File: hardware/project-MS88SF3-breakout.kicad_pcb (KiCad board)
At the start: 2 copper layers, 25.4 x 30.5 mm, 27 parts, among them J1 Conn_02x05_Odd_Even, J2 SM04B-SRSS-TB(LF)(SN), J3 USB4105-GF-A, J4 Conn_01x06_Male, J5 Conn_01x08_Male, SW1 SW_SPST, U1 MS88SF3

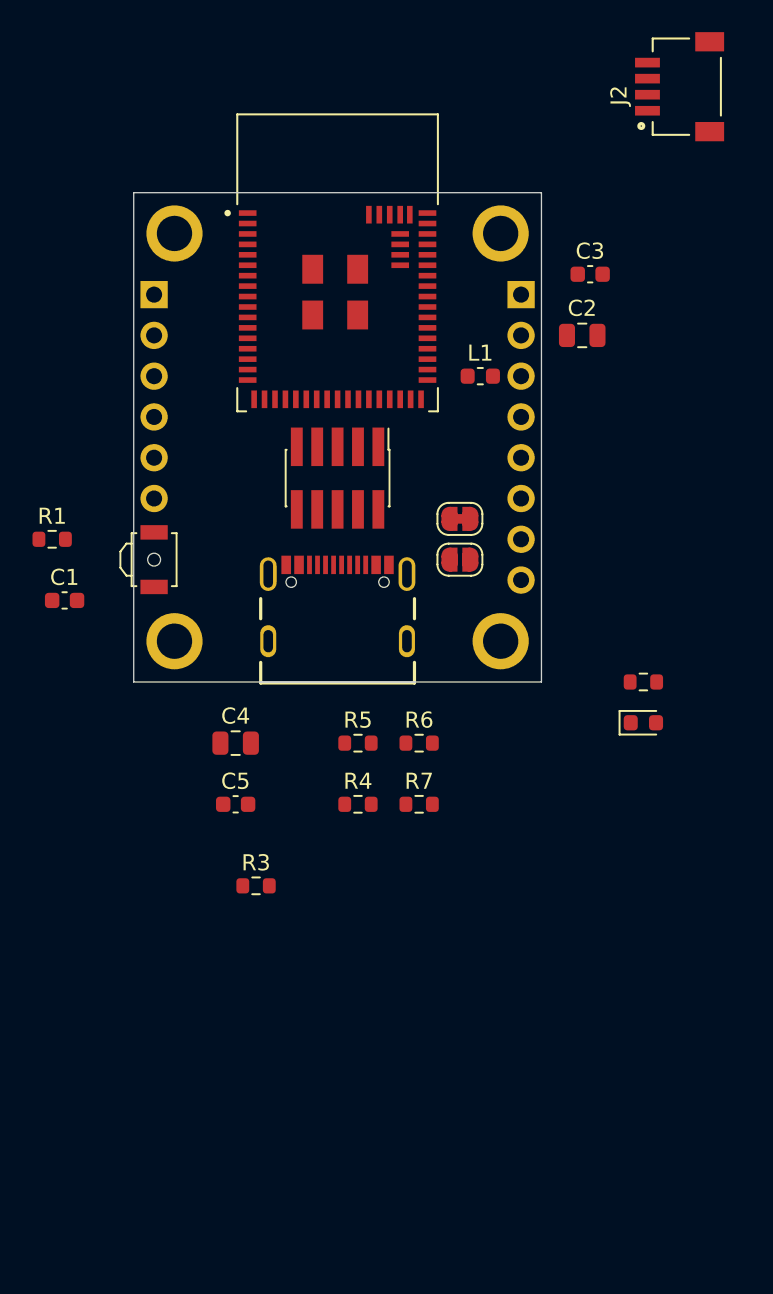
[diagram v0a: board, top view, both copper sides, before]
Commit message: Make it a feather shape
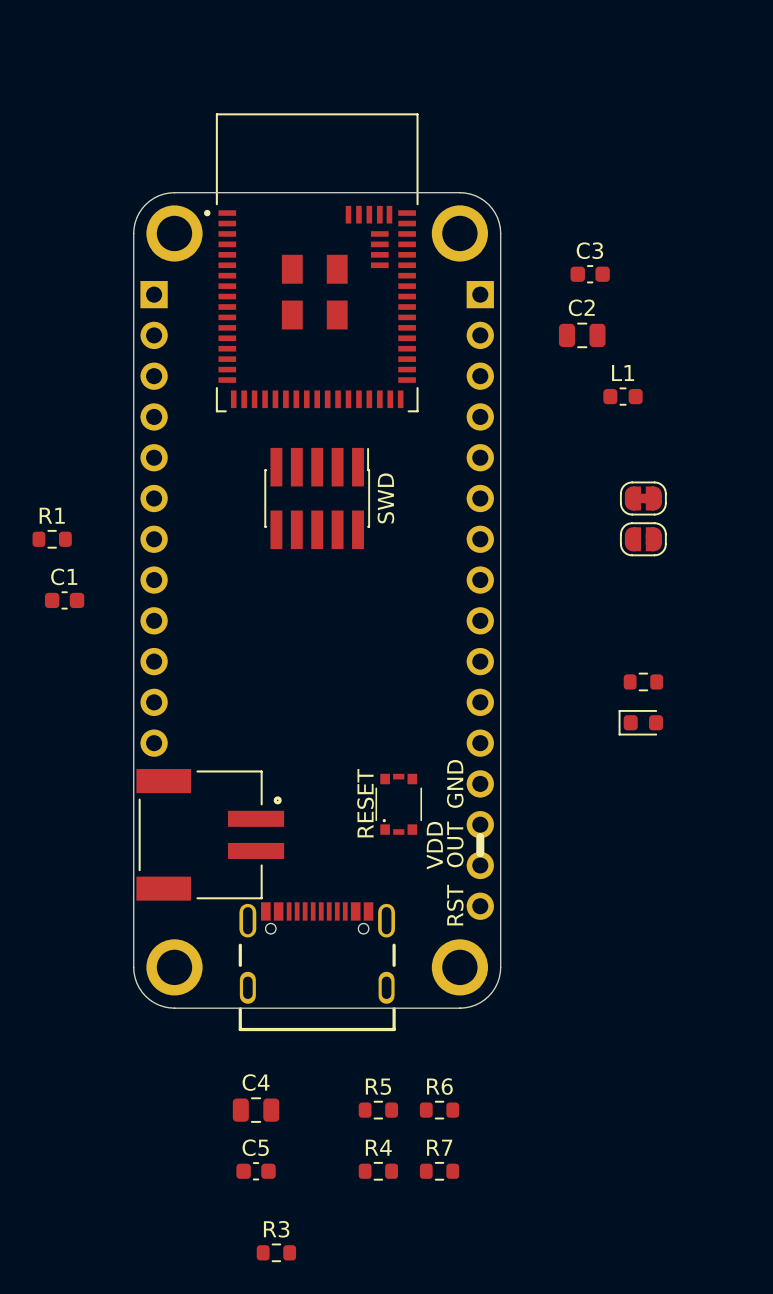
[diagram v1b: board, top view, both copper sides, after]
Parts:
- removed SW1: SW_SPST, Button_Switch_SMD:SW_SPST_B3U-3000P-B
- added S1: 435151014824, 435151014824:435151014824, F.Cu at (52.6, 118.9)
- J2: value SM04B-SRSS-TB(LF)(SN) -> S2B-PH-SM4-TB(LF)(SN); footprint SM04B-SRSS-TB(LF)(SN):JST_SM04B-SRSS-TB(LF)(SN) -> S2B-PH-SM4-TB(LF)(SN):JST_S2B-PH-SM4-TB(LF)(SN)
- J4: value Conn_01x06_Male -> Conn_01x12_Male; footprint Connector_PinHeader_2.54mm:PinHeader_1x06_P2.54mm_Vertical -> Connector_PinHeader_2.54mm:PinHeader_1x12_P2.54mm_Vertical; moved to B.Cu
- J5: value Conn_01x08_Male -> Conn_01x16_Male; footprint Connector_PinHeader_2.54mm:PinHeader_1x08_P2.54mm_Vertical -> Connector_PinHeader_2.54mm:PinHeader_1x16_P2.54mm_Vertical; moved to B.Cu
- moved J2 52.6 mm to (43.7, 120.8), turned to 270 degrees
- moved R3 22.9 mm to (45.0, 146.8)
- moved C4 22.9 mm to (43.7, 137.9)
- moved C5 22.9 mm to (43.7, 141.7)
- moved R4 22.9 mm to (51.3, 141.7)
- moved R5 22.9 mm to (51.3, 137.9)
- moved R6 22.9 mm to (55.1, 137.9)
- moved R7 22.9 mm to (55.1, 141.7)
- moved J3 21.6 mm to (47.5, 130.3)
- moved H4 20.5 mm to (56.4, 129.0)
- moved H3 20.3 mm to (38.6, 129.0)
- moved JP2 11.5 mm to (67.8, 102.4)
- moved JP1 11.5 mm to (67.8, 99.8)
- moved L1 8.98 mm to (66.5, 93.5)
- moved H2 2.54 mm to (56.4, 83.3)
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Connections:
- net Net-(JP1-Pad2) renamed /VDDH
- net Net-(U1-Pad49) renamed /SWDIO
- net Net-(U1-Pad50) renamed /SWCLK
- C1 pad 1: Net-(C1-Pad1) -> /RESET
- C1 pad 2: Net-(C1-Pad2) -> GND
- C2 pad 1: Net-(C2-Pad1) -> /VDD_nRF
- C2 pad 2: Net-(C2-Pad2) -> GND
- C3 pad 1: Net-(C3-Pad1) -> /VDD_nRF
- C3 pad 2: Net-(C3-Pad2) -> GND
- C4 pad 1: Net-(C4-Pad1) -> /VBUS
- C4 pad 2: Net-(C4-Pad2) -> GND
- C5 pad 1: Net-(C5-Pad1) -> /VBUS
- C5 pad 2: Net-(C5-Pad2) -> GND
- D1 pad 1: Net-(D1-Pad1) -> GND
- H1 pad 1: Net-(H1-Pad1) -> GND
- H2 pad 1: Net-(H2-Pad1) -> GND
- H3 pad 1: Net-(H3-Pad1) -> GND
- H4 pad 1: Net-(H4-Pad1) -> GND
- J1 pad 1: Net-(J1-Pad1) -> /VDD_nRF
- J1 pad 10: Net-(J1-Pad10) -> /RESET
- J1 pad 9: Net-(J1-Pad9) -> GND
- J3 pad A1_B12: Net-(J3-PadA1_B12) -> GND
- J3 pad A4_B9: Net-(J3-PadA4_B9) -> /VBUS
- J3 pad A5: Net-(J3-PadA5) -> /CC1
- J3 pad A6: Net-(J3-PadA6) -> /D+
- J3 pad A7: Net-(J3-PadA7) -> /D-
- J3 pad B1_A12: Net-(J3-PadA1_B12) -> GND
- J3 pad B4_A9: Net-(J3-PadA4_B9) -> /VBUS
- J3 pad B5: Net-(J3-PadB5) -> /CC2
- J3 pad B6: Net-(J3-PadB6) -> /D+
- J3 pad B7: Net-(J3-PadB7) -> /D-
- J3 pad S1: Net-(J3-PadS1) -> GND
- J3 pad S2: Net-(J3-PadS1) -> GND
- J3 pad S3: Net-(J3-PadS1) -> GND
- J3 pad S4: Net-(J3-PadS1) -> GND
- JP2 pad 1: /VDD_OUT -> /VDD_nRF
- L1 pad 2: /VDD_OUT -> /VDD_nRF
- R1 pad 1: Net-(R1-Pad1) -> /VDD_nRF
- R1 pad 2: Net-(R1-Pad2) -> /RESET
- R2 pad 1: Net-(R2-Pad1) -> Net-(D1-Pad2)
- R2 pad 2: Net-(R2-Pad2) -> /VBUS
- R3 pad 1: /VBUS_nRF -> /VBUS
- R3 pad 2: /VBUS_CONN -> /VBUS_nRF
- R4 pad 1: Net-(R4-Pad1) -> /CC1
- R4 pad 2: Net-(R4-Pad2) -> GND
- R5 pad 1: Net-(R5-Pad1) -> /CC2
- R5 pad 2: Net-(R5-Pad2) -> GND
- R6 pad 1: Net-(R6-Pad1) -> /D_P
- R6 pad 2: Net-(R6-Pad2) -> /D+
- R7 pad 1: Net-(R7-Pad1) -> /D_N
- R7 pad 2: Net-(R7-Pad2) -> /D-
- U1 pad 31: /VDD_OUT -> /VDD_nRF
- U1 pad 36: Net-(U1-Pad36) -> /D_N
- U1 pad 37: Net-(U1-Pad37) -> /D_P
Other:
- board size 25.4 x 30.5 mm -> 22.9 x 50.8 mm
- board text added: "GND"
- board text added: "OUT"
- board text added: "RESET"
- board text added: "RST"
- board text added: "SWD"
- board text added: "VDD"

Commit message: Change the MS88SF3 module to the nRF52840
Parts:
- U1: value MS88SF3 -> MS88SF3_NRF52840; footprint MS88SF3:MODULE_MS88SF3 -> MS88SF3_NRF52840:MODULE_MS88SF3_NRF52840
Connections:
- U1 pad 33: Net-(U1-Pad2) -> /DCCH
- U1 pad 38: Net-(U1-Pad2) -> Net-(U1-Pad38)
- U1 pad 43: Net-(U1-Pad2) -> Net-(U1-Pad43)
- U1 pad 48: Net-(U1-Pad2) -> Net-(U1-Pad48)
- U1 pad 58: Net-(U1-Pad2) -> Net-(U1-Pad58)
- U1 pad 60: Net-(U1-Pad2) -> Net-(U1-Pad60)

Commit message: Everything connected
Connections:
- net Net-(J4-Pad3) renamed /AIN1
- net Net-(U1-Pad2) renamed /P1.11
- net Net-(U1-Pad3) renamed /P1.12
- J1 pad 2: Net-(J1-Pad2) -> /SWDIO
- J1 pad 3: Net-(J1-Pad3) -> GND
- J1 pad 4: Net-(J1-Pad4) -> /SWCLK
- J1 pad 5: Net-(J1-Pad5) -> GND
- J1 pad 6: Net-(J1-Pad6) -> /TX
- J1 pad 8: Net-(J1-Pad8) -> /RX
- J2 pad 1: Net-(J2-Pad1) -> /VDD_nRF
- J2 pad 2: Net-(J2-Pad2) -> GND
- J2 pad S1: Net-(J2-PadS1) -> GND
- J2 pad S2: Net-(J2-PadS1) -> GND
- J4 pad 1: Net-(J4-Pad1) -> /P1.10
- J4 pad 10: Net-(J4-Pad10) -> /VBUS
- J4 pad 12: Net-(J4-Pad12) -> /VDD_nRF
- J4 pad 2: Net-(J4-Pad2) -> /P1.14
- J4 pad 4: Net-(J4-Pad4) -> /P1.13
- J4 pad 5: Net-(J4-Pad5) -> /P1.15
- J4 pad 6: Net-(J4-Pad6) -> /AIN0
- J4 pad 7: Net-(J4-Pad7) -> /AIN5
- J4 pad 8: Net-(J4-Pad8) -> /AIN3
- J4 pad 9: Net-(J4-Pad9) -> /AIN2
- J5 pad 1: Net-(J5-Pad1) -> /NFC1
- J5 pad 10: Net-(J5-Pad10) -> /P0.15
- J5 pad 11: Net-(J5-Pad11) -> /P0.13
- J5 pad 12: Net-(J5-Pad12) -> /P0.19
- J5 pad 13: Net-(J5-Pad13) -> GND
- J5 pad 14: Net-(J5-Pad14) -> /VDD_nRF
- J5 pad 15: Net-(J5-Pad15) -> /VDD_nRF
- J5 pad 16: Net-(J5-Pad16) -> /RESET
- J5 pad 2: Net-(J5-Pad2) -> /NFC2
- J5 pad 3: Net-(J5-Pad3) -> /TX
- J5 pad 4: Net-(J5-Pad4) -> /RX
- J5 pad 5: Net-(J5-Pad5) -> /P0.25
- J5 pad 6: Net-(J5-Pad6) -> /P0.22
- J5 pad 7: Net-(J5-Pad7) -> /P0.23
- J5 pad 8: Net-(J5-Pad8) -> /P0.21
- J5 pad 9: Net-(J5-Pad9) -> /P0.17
- L1 pad 1: /DCCH -> /VDD_nRF
- L1 pad 2: /VDD_nRF -> /DCCH
- U1 pad 10: Net-(U1-Pad10) -> /AIN5
- U1 pad 15: Net-(U1-Pad15) -> /AIN3
- U1 pad 16: Net-(U1-Pad16) -> /AIN2
- U1 pad 38: Net-(U1-Pad38) -> /P0.19
- U1 pad 39: Net-(U1-Pad39) -> /P0.13
- U1 pad 4: Net-(U1-Pad4) -> /P1.10
- U1 pad 40: Net-(U1-Pad40) -> /P0.15
- U1 pad 41: Net-(U1-Pad41) -> /P0.17
- U1 pad 42: Net-(U1-Pad42) -> /P0.21
- U1 pad 43: Net-(U1-Pad43) -> /P0.23
- U1 pad 45: Net-(U1-Pad45) -> /P0.22
- U1 pad 48: Net-(U1-Pad48) -> /P0.25
- U1 pad 5: Net-(U1-Pad5) -> /P1.14
- U1 pad 55: Net-(U1-Pad55) -> /NFC1
- U1 pad 56: Net-(U1-Pad56) -> /NFC2
- U1 pad 7: Net-(U1-Pad7) -> /P1.13
- U1 pad 8: Net-(U1-Pad8) -> /P1.15
- U1 pad 9: Net-(U1-Pad9) -> /AIN0

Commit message: Half routing done
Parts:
- removed C3: 100nF, Capacitor_SMD:C_0603_1608Metric
- added C6: 4.7uF, Capacitor_SMD:C_0805_2012Metric, F.Cu at (54.1, 96.8)
- moved R3 48.8 mm to (52.3, 98.6), turned to 90 degrees
- moved JP1 25.0 mm to (42.9, 98.0), turned to 90 degrees
- moved R4 23.7 mm to (49.8, 118.1), turned to 90 degrees
- moved JP2 22.8 mm to (45.5, 98.0), turned to 90 degrees
- moved R1 22.2 mm to (52.1, 109.5), turned to 180 degrees
- moved C5 22.1 mm to (51.8, 121.2)
- moved R7 20.6 mm to (47.2, 122.7), turned to 270 degrees
- moved C1 20.4 mm to (52.1, 108.0)
- moved R5 19.8 mm to (51.3, 118.1), turned to 90 degrees
- moved D1 18.7 mm to (53.8, 126.2), turned to 90 degrees
- moved C4 17.2 mm to (52.1, 122.9)
- moved R6 16.5 mm to (48.8, 122.7), turned to 270 degrees
- moved C2 16.5 mm to (49.5, 97.5), turned to 180 degrees
- moved R2 15.6 mm to (53.8, 118.1), turned to 90 degrees
- moved L1 15.4 mm to (51.3, 95.8)
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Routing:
- net /D_P: track 0.00 -> 35.4 mm
- net /D_N: track 0.00 -> 34.6 mm
- net GND: track 0.00 -> 25.0 mm, vias 0 -> 16
- net /AIN2: track 0.00 -> 17.7 mm
- net /AIN5: track 0.00 -> 16.4 mm
- net /AIN3: track 0.00 -> 15.8 mm
- net /AIN0: track 0.00 -> 14.5 mm
- net /P1.15: track 0.00 -> 12.7 mm
- net /P1.13: track 0.00 -> 10.9 mm
- net /VBUS: track 0.00 -> 9.87 mm, vias 0 -> 2
- net /CC1: track 0.00 -> 8.97 mm, vias 0 -> 2
- net /CC2: track 0.00 -> 7.47 mm
- net Net-(D1-Pad2): track 0.00 -> 7.18 mm
- net /P1.14: track 0.00 -> 6.95 mm
- net /VBUS_nRF: track 0.00 -> 6.18 mm
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- added copper zone on F.Cu, net /VBUS
- added copper zone on In2.Cu, net /VDD_nRF
- added copper zone on In1.Cu, net GND
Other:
- copper layers 2 -> 4
- net class Smallest added: clearance 0.127, trace_width 0.127, via_dia 0.8, via_drill 0.4
- rule trace_min: 0.2 -> 0.127
- board text added: "19"
- board text added: "25"
- board text added: "P0"
- board text added: "SB1"
- board text added: "SB2"

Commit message: USB route
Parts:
- moved C1 20.9 mm to (72.6, 104.4)
- moved R1 20.9 mm to (72.6, 105.9)
- moved S1 20.9 mm to (72.1, 109.5)
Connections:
- J5 pad 3: /TX -> /RX
- J5 pad 4: /RX -> /TX
- U1 pad 6: Net-(U1-Pad6) -> /AIN1
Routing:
- net /SWDIO: track 0.00 -> 40.1 mm, vias 0 -> 2
- net /SWCLK: track 0.00 -> 31.2 mm, vias 0 -> 2
- net /NFC2: track 0.00 -> 13.7 mm, vias 0 -> 1
- net /NFC1: track 0.00 -> 11.4 mm, vias 0 -> 1
- net /TX: track 0.00 -> 10.0 mm
- net /AIN1: track 0.00 -> 9.07 mm
- net /RX: track 0.00 -> 8.87 mm
- net GND: track 25.0 -> 29.6 mm, vias 16 -> 19
- net /VDD_nRF: track 5.05 -> 8.87 mm, vias 1 -> 2

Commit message: Routing done
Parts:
- moved S1 30.1 mm to (42.2, 111.8)
- moved R1 28.1 mm to (45.0, 111.0), turned to 90 degrees
- moved C1 27.0 mm to (46.5, 111.0), turned to 270 degrees
- moved JP1 2.54 mm to (45.5, 98.0)
- moved JP2 2.54 mm to (42.9, 98.0)
- moved J1 0.76 mm to (47.5, 103.9)
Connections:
- J5 pad 1: /NFC1 -> /P0.25
- J5 pad 11: /P0.13 -> /P0.17
- J5 pad 12: /P0.19 -> /P0.21
- J5 pad 2: /NFC2 -> /NFC1
- J5 pad 3: /RX -> /NFC2
- J5 pad 4: /TX -> /RX
- J5 pad 5: /P0.25 -> /P0.22
- J5 pad 6: /P0.22 -> /TX
- J5 pad 8: /P0.21 -> /P0.19
- J5 pad 9: /P0.17 -> /P0.13
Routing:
- net /RESET: track 0.00 -> 55.1 mm, vias 0 -> 1
- net /VBUS: track 9.87 -> 43.0 mm, vias 2 -> 5
- net /P0.21: track 0.00 -> 32.5 mm, vias 0 -> 1
- net /P0.17: track 0.00 -> 28.4 mm, vias 0 -> 1
- net /RX: track 8.87 -> 37.1 mm, vias 0 -> 1
- net /P0.15: track 0.00 -> 24.6 mm, vias 0 -> 1
- net /TX: track 10.0 -> 34.6 mm, vias 0 -> 1
- net /P0.13: track 0.00 -> 21.3 mm, vias 0 -> 1
- net /VDDH: track 0.00 -> 19.2 mm, vias 0 -> 4
- net /P0.19: track 0.00 -> 18.0 mm, vias 0 -> 1
- net /P0.23: track 0.00 -> 17.1 mm
- net /P0.22: track 0.00 -> 13.3 mm
- net /VBUS_nRF: track 6.18 -> 15.0 mm, vias 0 -> 2
- net GND: track 29.6 -> 36.1 mm, vias 19 -> 22
- net /P0.25: track 0.00 -> 5.72 mm
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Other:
- board text added: "-"
- board text added: "09"
- board text added: "10"
- board text added: "13"
- board text added: "14"
- board text added: "15"
- board text added: "17"
- board text added: "21"
- board text added: "22"
- board text added: "23"
- board text added: "A0"
- board text added: "A1"
- board text added: "A2"
- board text added: "A3"
- board text added: "A5"
- board text added: "François Gervais 27 août 2022 v1.0.0"
- board text added: "NFC1"
- board text added: "NFC2"
- board text added: "P0.20"
- board text added: "P0.24"
- board text added: "P1"
- board text added: "RX"
- board text added: "TX"
- board text added: "USB"

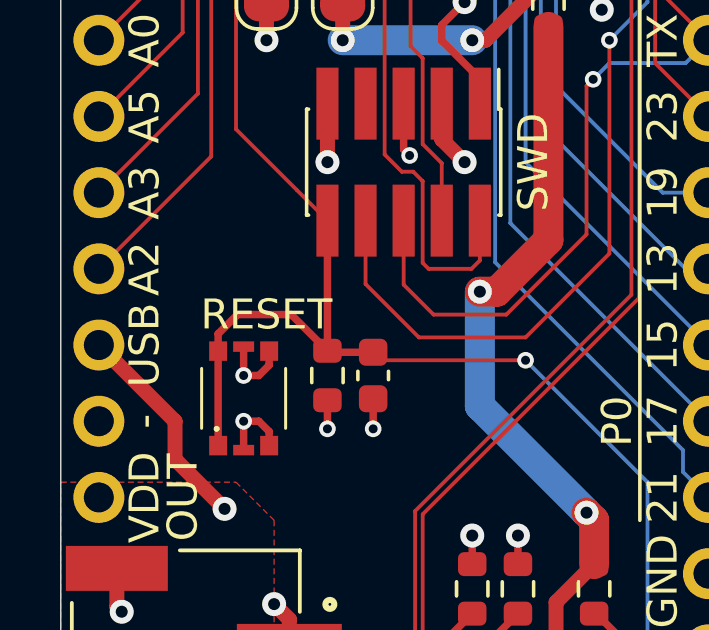
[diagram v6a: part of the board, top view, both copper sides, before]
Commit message: Clean up schematic
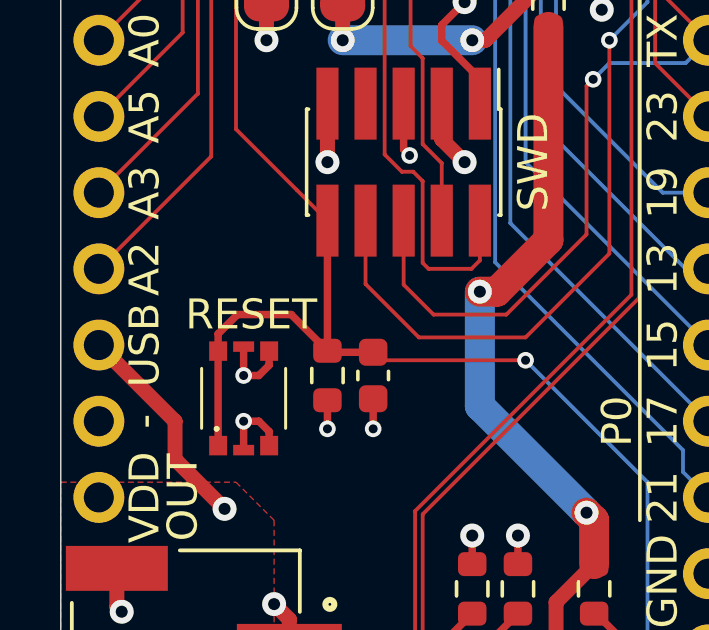
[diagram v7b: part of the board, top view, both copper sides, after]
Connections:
- net /P1.11 renamed Net-(U1-Pad2)
- net /P1.12 renamed Net-(U1-Pad3)

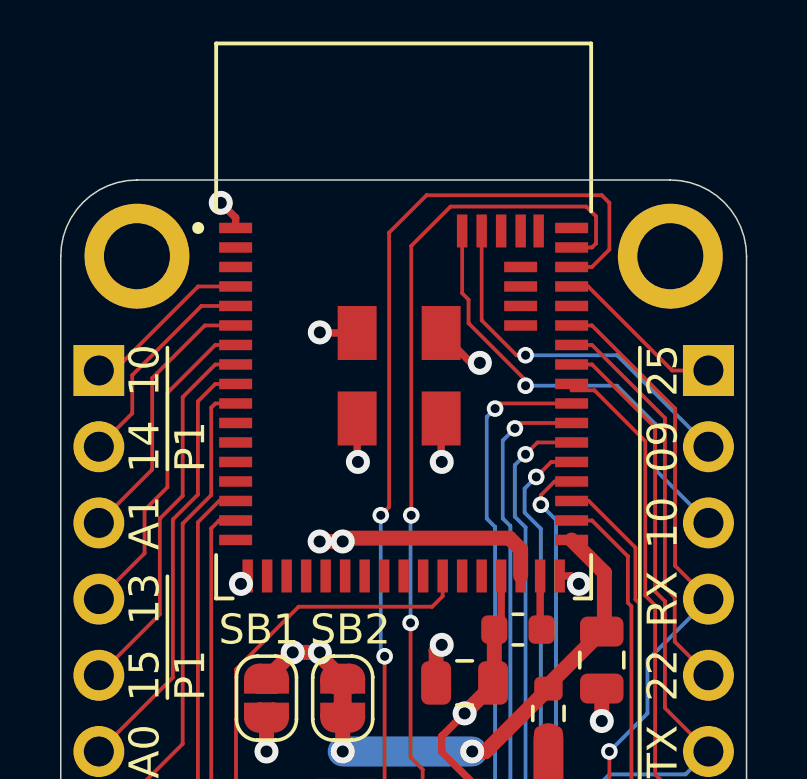
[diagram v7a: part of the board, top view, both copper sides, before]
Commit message: Ground fill under the module
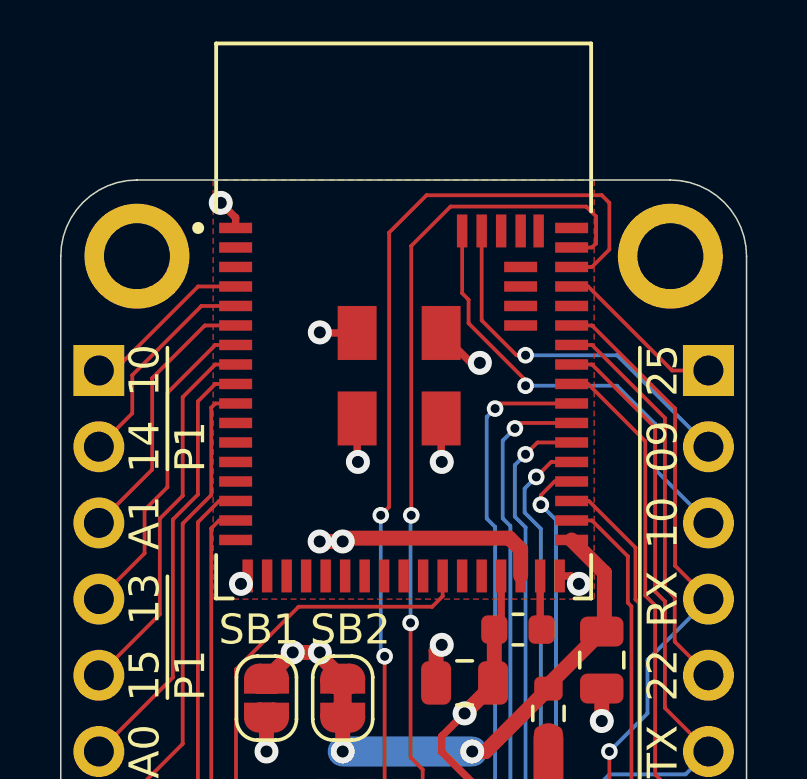
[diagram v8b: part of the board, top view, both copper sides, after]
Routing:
- added copper zone on F.Cu, net GND
